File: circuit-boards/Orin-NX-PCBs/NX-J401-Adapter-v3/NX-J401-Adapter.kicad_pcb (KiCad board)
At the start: 4 copper layers, 109.9 x 79 mm, 50 parts, among them J1 Power, J10 MIPI, J11 HDMI, J2 CAN-NX, J3 NX-BUTTON, J4 CONSOLE, J5 18V_OUT, J6 CAN-NX, J7 CAN-NX, J8 MIPI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

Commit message: Interim checkin of NX Adapter board
Signed-off-by: Scott Berman <scott.berman@bluerivertech.com>
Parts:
- J11, J9: footprint NX-J401-Adapter:HDMI_A_Molex_208658-1001_Horizontal -> NX-J401-Adapter:SWITCHCRAFT_RAVHD19ETR
- moved J9 5.67 mm to (239.2, 148.5), turned to 0 degrees
- moved J11 5.57 mm to (254.4, 148.5), turned to 0 degrees
- moved J8 1.15 mm to (225.6, 125.6)
- moved J10 0.67 mm to (225.6, 100.7)
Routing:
- net /MIPI-HDMI-2/CAM_D1_P: track 0.00 -> 72.7 mm
- net /MIPI-HDMI-2/CAM_CK_P: track 0.00 -> 72.5 mm, vias 0 -> 1
- net /MIPI-HDMI-2/CAM_CK_N: track 0.00 -> 72.2 mm, vias 0 -> 1
- net /MIPI-HDMI-2/CAM_D1_N: track 0.00 -> 71.0 mm
- net /MIPI-HDMI-2/CAM_D0_P: track 0.00 -> 64.5 mm, vias 0 -> 1
- net /MIPI-HDMI-2/CAM_D0_N: track 0.00 -> 64.4 mm, vias 0 -> 1
- net /MIPI-HDMI-1/CAM_CK_P: track 0.00 -> 36.9 mm, vias 0 -> 1
- net /MIPI-HDMI-1/CAM_D1_P: track 0.00 -> 36.2 mm
- net /MIPI-HDMI-1/CAM_CK_N: track 0.00 -> 36.0 mm, vias 0 -> 1
- net /MIPI-HDMI-1/CAM_D1_N: track 0.00 -> 34.6 mm
- net /MIPI-HDMI-1/CAM_D0_P: track 0.00 -> 25.9 mm, vias 0 -> 1
- net /MIPI-HDMI-1/CAM_D0_N: track 0.00 -> 25.1 mm, vias 0 -> 1
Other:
- board text added: "D"
- board text added: "H"
- board text added: "NOTES: 1. MATERIAL: JLCPCB JLC04161H-3313A"
- board text added: "Param | Size ---------------------------------------------- Z | 100 ohm S | 10 mil D | 10 mil W | 9.79 mil T | 1.38 mil H | 8.12 mil (2x3313 57% 4.2 mil) JLCPCB: JLC04161H-3313A"
- board text added: "S"
- board text added: "T"
- board text added: "W"

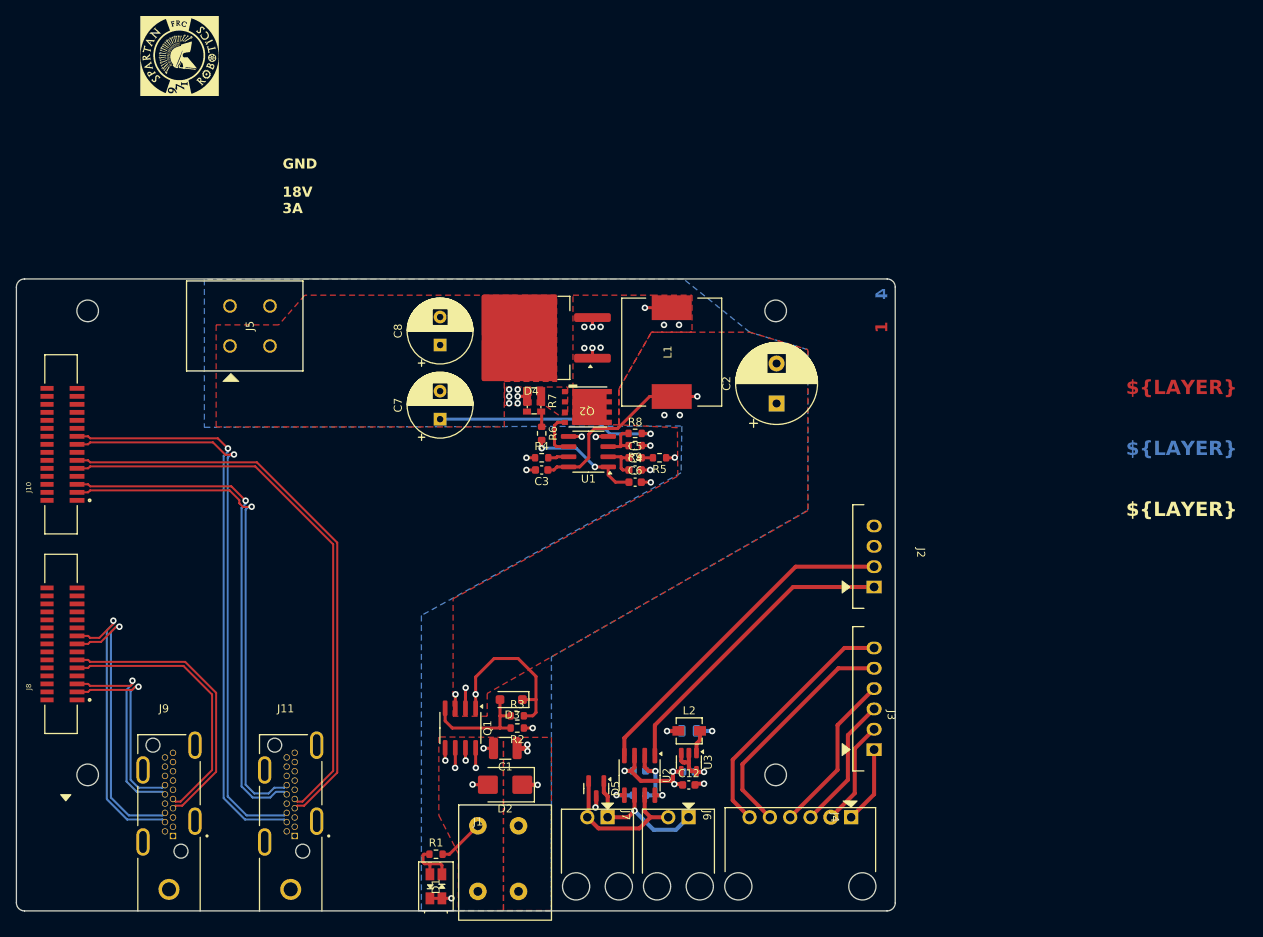
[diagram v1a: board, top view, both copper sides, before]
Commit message: NX Adapter interim checking
Signed-off-by: Scott <sgberman1@gmail.com>
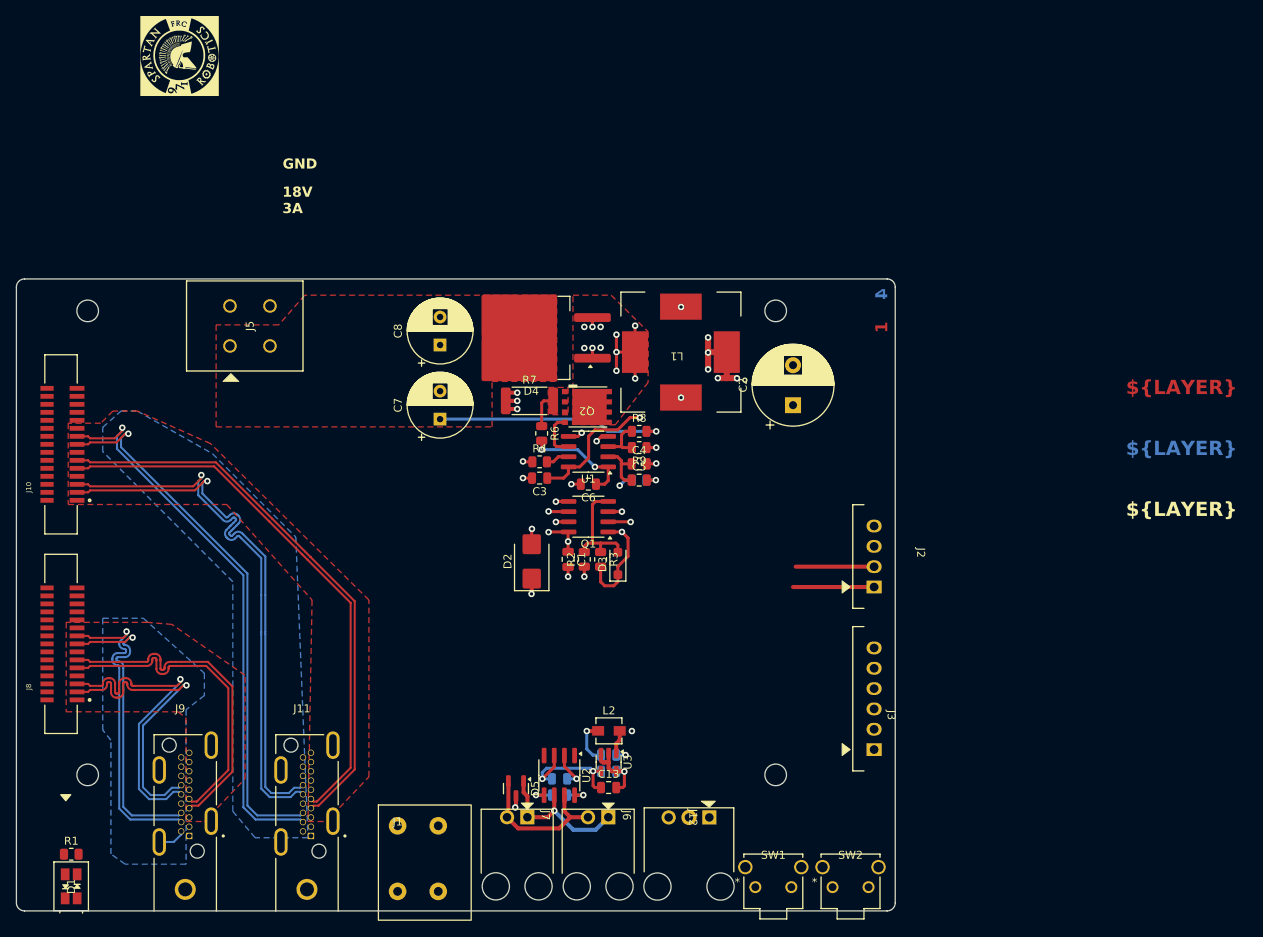
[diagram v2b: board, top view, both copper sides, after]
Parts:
- removed C12: 22uF-20%-0603, Capacitor_SMD:C_0603_1608Metric
- removed J4: CONSOLE, NX-J401-Adapter:70555-0005
- added C14: 0.22uF-10%-50V-0805, Capacitor_SMD:C_0805_2012Metric, B.Cu at (288.0, 144.5)
- added J12: CONSOLE, NX-J401-Adapter:70555-0002, F.Cu at (304.2, 147.3)
- added SW1: RESET, NX-J401-Adapter:SW_TL1105VF100Q_EWI, F.Cu at (312.5, 156.0)
- added SW2: RECOVERY, NX-J401-Adapter:SW_TL1105VF100Q_EWI, F.Cu at (322.1, 156.0)
- C1: value 22uF-25V-10%-1210 -> 22uF-20%-25V-0805; footprint Capacitor_SMD:C_1210_3225Metric -> Capacitor_SMD:C_0805_2012Metric
- C10, C3: value 0.1uF-10%-50V-0603 -> 0.22uF-10%-50V-0805; footprint Capacitor_SMD:C_0603_1608Metric -> Capacitor_SMD:C_0805_2012Metric
- C11: value 0.1uF-10%-50V-0603 -> 22uF-20%-25V-0805; footprint Capacitor_SMD:C_0603_1608Metric -> Capacitor_SMD:C_0805_2012Metric
- C13: value 22uF-20%-0603 -> 22uF-20%-25V-0805; footprint Capacitor_SMD:C_0603_1608Metric -> Capacitor_SMD:C_0805_2012Metric; moved to F.Cu
- C4: value 0.01uF-10%-50V-0603 -> 0.01uF-10%-50V-0805; footprint Capacitor_SMD:C_0603_1608Metric -> Capacitor_SMD:C_0805_2012Metric
- C5: value 0.22uF-10%-50V-0603 -> 0.22uF-10%-50V-0805; footprint Capacitor_SMD:C_0603_1608Metric -> Capacitor_SMD:C_0805_2012Metric
- C6: value 10pF-5%-50V-0603 -> 10pF-5%-50V-0805; footprint Capacitor_SMD:C_0603_1608Metric -> Capacitor_SMD:C_0805_2012Metric
- L1: value 4.7 uH-8.4m-20% -> 6.8 uH-12m-20%; footprint NX-J401-Adapter:Bourns-SRP1265A -> NX-J401-Adapter:INDUCTOR_IHLE-5050FH-Vishay
- R1: value 4.99k-1%-0603 -> 4.99k-1%-0805; footprint Resistor_SMD:R_0603_1608Metric -> Resistor_SMD:R_0805_2012Metric
- R2, R9: value 1.0k-1%-0603 -> 1.05k-1%-0805; footprint Resistor_SMD:R_0603_1608Metric -> Resistor_SMD:R_0805_2012Metric
- R3: value 20.0k-1%-0603 -> 20.0k-1%-0805; footprint Resistor_SMD:R_0603_1608Metric -> Resistor_SMD:R_0805_2012Metric
- R4: value 64.9k-1%-0603 -> 59.0k-1%-0805; footprint Resistor_SMD:R_0603_1608Metric -> Resistor_SMD:R_0805_2012Metric
- R5: value 1.0k-1%-0603 -> 1.05k-1%-0805; footprint Resistor_SMD:R_0603_1608Metric -> Resistor_SMD:R_0805_2012Metric; moved to B.Cu
- R6: value 100R-1%-0603 -> 100R-1%-0805; footprint Resistor_SMD:R_0603_1608Metric -> Resistor_SMD:R_0805_2012Metric
- R7: value 4.0m-1%-1W -> 4.0m-1%-2512; footprint Resistor_SMD:R_Shunt_Vishay_WSKW0612 -> Resistor_SMD:R_2512_6332Metric
- R8: value 13.3k-1%-0603 -> 14.0k-1%-0805; footprint Resistor_SMD:R_0603_1608Metric -> Resistor_SMD:R_0805_2012Metric
- moved D1 45.6 mm to (226.9, 155.9)
- moved R1 45.6 mm to (226.9, 151.9)
- moved Q1 30.9 mm to (291.6, 109.7), turned to 180 degrees
- moved D2 28.1 mm to (284.5, 115.3), turned to 90 degrees
- moved C1 24.9 mm to (289.1, 115.1), turned to -90 degrees
- moved R2 22.7 mm to (291.1, 115.1), turned to 90 degrees
- moved R3 22.2 mm to (293.1, 115.1), turned to -90 degrees
- moved D3 21.6 mm to (295.3, 115.6), turned to 90 degrees
- moved C9 10.5 mm to (294.1, 139.5)
- moved C13 10.2 mm to (294.1, 143.6)
- moved C10 10.2 mm to (288.0, 142.5)
- moved D5 10.0 mm to (282.5, 143.7)
- moved J1 10.0 mm to (267.7, 148.4)
- moved J6 10.0 mm to (292.8, 147.3)
- moved J7 10.0 mm to (282.7, 147.3)
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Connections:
- C1 pad 1: GND -> /Power Supply/V_{BAT}
- C1 pad 2: /Power Supply/V_{BAT} -> GND
- C10 pad 1: /NX CAN/+3V3 -> /NX CAN/+5V
- R6 pad 1: Net-(R6-Pad1) -> /Power Supply/Q_S
- R7 pad 1: /Power Supply/Q_S -> GND
- R7 pad 2: Net-(R6-Pad1) -> /Power Supply/Q_S
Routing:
- net /RTN: track 39.1 -> 0.00 mm
- net /NX CAN/CAN_RX: track 42.3 -> 9.80 mm
- net /~{REC}: track 31.5 -> 0.00 mm
- net /NX CAN/CAN_TX: track 38.4 -> 10.1 mm
- net /~{SYS_RESET}: track 20.4 -> 0.00 mm
- net /UART2_TXD: track 16.8 -> 0.00 mm
- net /MIPI-HDMI-1/CAM_D0_N: track 25.1 -> 39.2 mm
- net /MIPI-HDMI-1/CAM_D0_P: track 25.9 -> 40.0 mm
- net /UART2_RXD: track 13.2 -> 0.00 mm
- net /Power Supply/SW: track 9.88 -> 22.8 mm, vias 9 -> 11
- net Net-(D1A-Red-K): track 6.70 -> 0.00 mm
- net /MIPI-HDMI-1/CAM_D1_N: track 34.6 -> 39.9 mm
- net /MIPI-HDMI-1/CAM_D1_P: track 36.2 -> 41.6 mm
- net /Power Supply/V_{BAT}: track 17.3 -> 12.7 mm
- net /Power Supply/Q_S: track 0.00 -> 4.44 mm
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- added copper zone on B.Cu, net /MIPI-HDMI-1/GND_MIPI
- added copper zone on F.Cu, net /MIPI-HDMI-1/GND_MIPI
- added copper zone on B.Cu, net /MIPI-HDMI-2/GND_MIPI
- added copper zone on F.Cu, net /MIPI-HDMI-2/GND_MIPI
- removed copper zone on In1.Cu, net /MIPI-HDMI-1/GND_MIPI
- removed copper zone on In2.Cu, net /MIPI-HDMI-1/GND_MIPI
- removed copper zone on F.Cu, net /Power Supply/V_IN
- removed copper zone on In1.Cu, net /Power Supply/V_IN
- removed copper zone on F.Cu, net /Power Supply/V_{BAT}
- removed copper zone on In1.Cu, net /Power Supply/V_{BAT}
- removed copper zone on B.Cu, net GND
- removed copper zone on F.Cu, net GND
- removed copper zone on In1.Cu, net GND

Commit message: interim checkin of NX Adapter board
Signed-off-by: Scott Berman <scott.berman@bluerivertech.com>
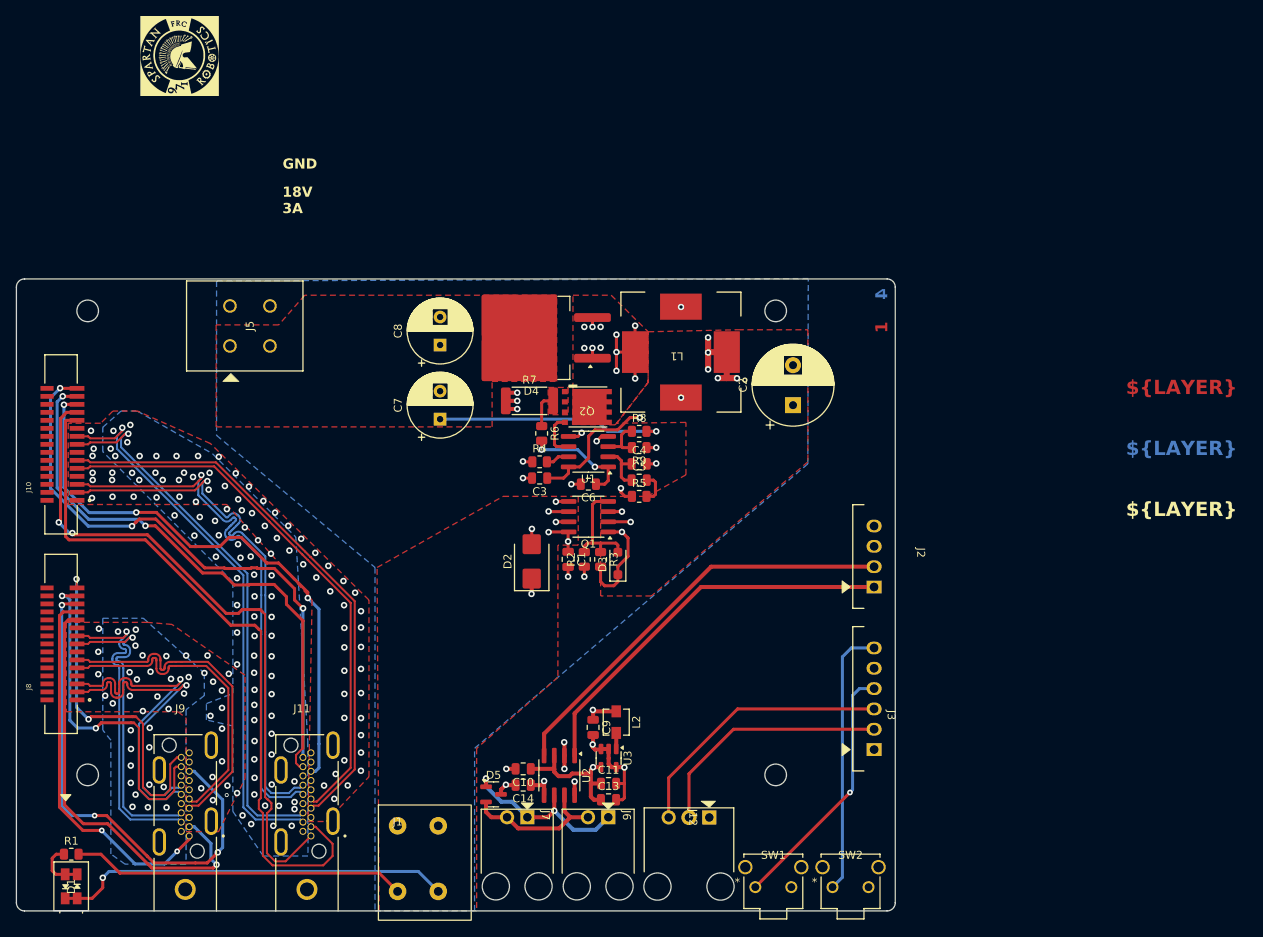
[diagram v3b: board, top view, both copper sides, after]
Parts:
- C10, C11, C14, C9, R5: moved to F.Cu
- moved C14 4.71 mm to (283.4, 143.3), turned to 180 degrees
- moved C10 4.71 mm to (283.4, 141.2), turned to 180 degrees
- moved C9 3.96 mm to (292.2, 136.1), turned to -90 degrees
- moved D5 2.90 mm to (279.7, 144.4), turned to 0 degrees
- moved R5 2.03 mm to (297.9, 107.2)
- moved C11 1.52 mm to (294.1, 143.1)
- moved C13 1.52 mm to (294.1, 145.1)
- moved L2 1.42 mm to (295.1, 135.4), turned to -90 degrees
- moved U3 0.51 mm to (294.1, 139.9)
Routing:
- net /MIPI-HDMI-2/PWR_DN_LS: track 0.00 -> 88.4 mm
- net /MIPI-HDMI-2/CAM_MCLK: track 0.00 -> 84.1 mm, vias 0 -> 2
- net /MIPI-HDMI-2/CAM_3V3: track 0.00 -> 73.2 mm, vias 0 -> 3
- net /MIPI-HDMI-2/CAM_SCL: track 0.00 -> 72.8 mm, vias 0 -> 3
- net /MIPI-HDMI-2/CAM_SDA: track 0.00 -> 71.0 mm, vias 0 -> 2
- net /MIPI-HDMI-1/CAM_SCL: track 0.00 -> 62.5 mm, vias 0 -> 3
- net /MIPI-HDMI-1/PWR_DN_LS: track 0.00 -> 53.4 mm, vias 0 -> 1
- net GND: track 21.8 -> 71.9 mm, vias 16 -> 17
- net /MIPI-HDMI-1/CAM_MCLK: track 0.00 -> 47.2 mm, vias 0 -> 2
- net /MIPI-HDMI-1/CAM_SDA: track 0.00 -> 44.5 mm, vias 0 -> 2
- net /MIPI-HDMI-1/CAM_3V3: track 0.00 -> 43.5 mm, vias 0 -> 2
- net /NX CAN/CAN_RX: track 9.80 -> 52.6 mm
- net /Power Supply/V_{BAT}: track 12.7 -> 54.5 mm
- net /NX CAN/CAN_TX: track 10.1 -> 49.3 mm
- net /UART2_TXD: track 0.00 -> 34.2 mm
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- added copper zone on In1.Cu, net /MIPI-HDMI-1/GND_MIPI
- added copper zone on In2.Cu, net /MIPI-HDMI-1/GND_MIPI
- added copper zone on In1.Cu, net /MIPI-HDMI-2/GND_MIPI
- added copper zone on In2.Cu, net /MIPI-HDMI-2/GND_MIPI
- added copper zone on F.Cu, net /Power Supply/V_IN
- added copper zone on In1.Cu, net /Power Supply/V_IN
- added copper zone on F.Cu, net /Power Supply/V_{BAT}
- added copper zone on In1.Cu, net /Power Supply/V_{BAT}
- added copper zone on In1.Cu, net /RTN
- added copper zone on In2.Cu, net /RTN
- added copper zone on B.Cu, net GND
